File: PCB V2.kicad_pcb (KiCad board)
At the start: 2 copper layers, 17 parts, among them J1 Conector IR, J10 Conector ultrassonico esquerdo, J11 Conector ultrassonico central, J12 Conector ultrassonico direito, J13 Conector LED Extra, J14 Conector LORA, J15 ENCO_SW_Esq, J16 ENCO_SW_Dir, J18 LEDs, J2 Conector bluetooth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

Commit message: feat: finalizacao da versao 2 da pcb
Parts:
- added G***: LOGO, LOGO, F.Cu at (142.1, 37.9)
- added REF**: PinHeader_1x08_P2.54mm_Vertical, Connector_PinHeader_2.54mm:PinHeader_1x08_P2.54mm_Vertical, F.Cu at (157.4, 66.0)
- added REF**: MountingHole_3.2mm_M3, MountingHole:MountingHole_3.2mm_M3, F.Cu at (185.4, 36.6)
- added REF**: MountingHole_3.2mm_M3, MountingHole:MountingHole_3.2mm_M3, F.Cu at (185.4, 115.8)
- added REF**: PinHeader_1x08_P2.54mm_Vertical, Connector_PinHeader_2.54mm:PinHeader_1x08_P2.54mm_Vertical, F.Cu at (116.7, 114.3)
- added REF**: PinSocket_2x03_P2.54mm_Vertical, Connector_PinSocket_2.54mm:PinSocket_2x03_P2.54mm_Vertical, F.Cu at (154.9, 86.4)
- added REF**: PinHeader_1x08_P2.54mm_Vertical, Connector_PinHeader_2.54mm:PinHeader_1x08_P2.54mm_Vertical, F.Cu at (162.4, 114.3)
- added REF**: PinHeader_1x08_P2.54mm_Vertical, Connector_PinHeader_2.54mm:PinHeader_1x08_P2.54mm_Vertical, F.Cu at (134.5, 66.0)
- added REF**: MountingHole_3.2mm_M3, MountingHole:MountingHole_3.2mm_M3, F.Cu at (88.9, 36.6)
- added REF**: MountingHole_3.2mm_M3, MountingHole:MountingHole_3.2mm_M3, F.Cu at (88.9, 150.9)
- added REF**: PinHeader_1x10_P2.54mm_Vertical, Connector_PinHeader_2.54mm:PinHeader_1x10_P2.54mm_Vertical, F.Cu at (107.6, 66.0)
- added REF**: PinHeader_2x18_P2.54mm_Vertical, Connector_PinHeader_2.54mm:PinHeader_2x18_P2.54mm_Vertical, F.Cu at (182.8, 66.0)
- added REF**: PinHeader_1x08_P2.54mm_Vertical, Connector_PinHeader_2.54mm:PinHeader_1x08_P2.54mm_Vertical, F.Cu at (139.6, 114.3)
- J7, J8: moved to B.Cu
- moved J12 20.6 mm to (144.6, 50.8)
- moved J14 20.4 mm to (165.4, 50.8)
- moved R1 10.2 mm to (88.9, 58.2), turned to 0 degrees
- moved J7 2.03 mm to (99.1, 158.0), turned to 90 degrees
- moved J8 2.03 mm to (167.6, 158.0), turned to 90 degrees
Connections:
- J7 pad 1: 5V_Sen -> Earth
- J7 pad 2: Earth -> 5V_Sen
- J8 pad 1: 5V_Sen -> Earth
- J8 pad 2: Earth -> 5V_Sen
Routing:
- net Earth: track 80.4 -> 431.3 mm, vias 6 -> 19
- net 5V_Sen: track 90.7 -> 382.3 mm, vias 0 -> 14
- net IR2: track 0.00 -> 258.6 mm, vias 0 -> 8
- net ENCODER_Esq_1: track 0.00 -> 248.3 mm, vias 0 -> 8
- net IR1: track 0.00 -> 232.6 mm, vias 0 -> 4
- net LED_Extra: track 0.00 -> 172.0 mm, vias 0 -> 6
- net Servo: track 0.00 -> 136.3 mm, vias 0 -> 4
- net A_SDA: track 0.00 -> 135.2 mm, vias 0 -> 4
- net A_SCL: track 0.00 -> 134.3 mm, vias 0 -> 2
- net ENCODER_Dir_2: track 0.00 -> 130.3 mm, vias 0 -> 2
- net MD1: track 0.00 -> 129.8 mm, vias 0 -> 2
- net ENCODER_Dir_1: track 0.00 -> 124.8 mm, vias 0 -> 2
- net MD2: track 0.00 -> 124.5 mm, vias 0 -> 2
- net ME1: track 0.00 -> 120.9 mm, vias 0 -> 4
- net ME2: track 0.00 -> 116.5 mm, vias 0 -> 4
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- added copper zone on B.Cu, net Earth
- added copper zone on F.Cu, net Earth
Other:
- board outline added: 113.8 x 133.6 mm
- board text added: "+5V"
- board text added: "A"
- board text added: "B"
- board text added: "CONECTOR ACELEROMETRO"
- board text added: "CONECTOR BLUETOOTH"
- board text added: "CONECTOR DO SERVO"
- board text added: "CONECTOR ENCODER - DIR"
- board text added: "CONECTOR ENCODER - ESQ"
- board text added: "CONECTOR INFRAVERMELHO"
- board text added: "CONECTOR LED EXTRA"
- board text added: "CONECTOR LEDS FAROIS"
- board text added: "CONECTOR LORA"
- board text added: "CONECTOR ULTRASSONICO - CEN"
- board text added: "CONECTOR ULTRASSONICO - DIR"
- board text added: "CONECTOR ULTRASSONICO - ESQ"
- board text added: "ENTRADA BATERIA SENSORES"
- board text added: "FAROIS"
- board text added: "FREIOS"
- board text added: "GND"
- board text added: "M3"
- board text added: "PONTE H - DIR"
- board text added: "PONTE H - ESQ"
- board text added: "R 220 OHMS"
- board text added: "SERVO"
- board text added: "SETA DIR"
- board text added: "SETA ESQ"
- board text added: "SHIELD ARDUINO MEGA"
- board text added: "VCC"

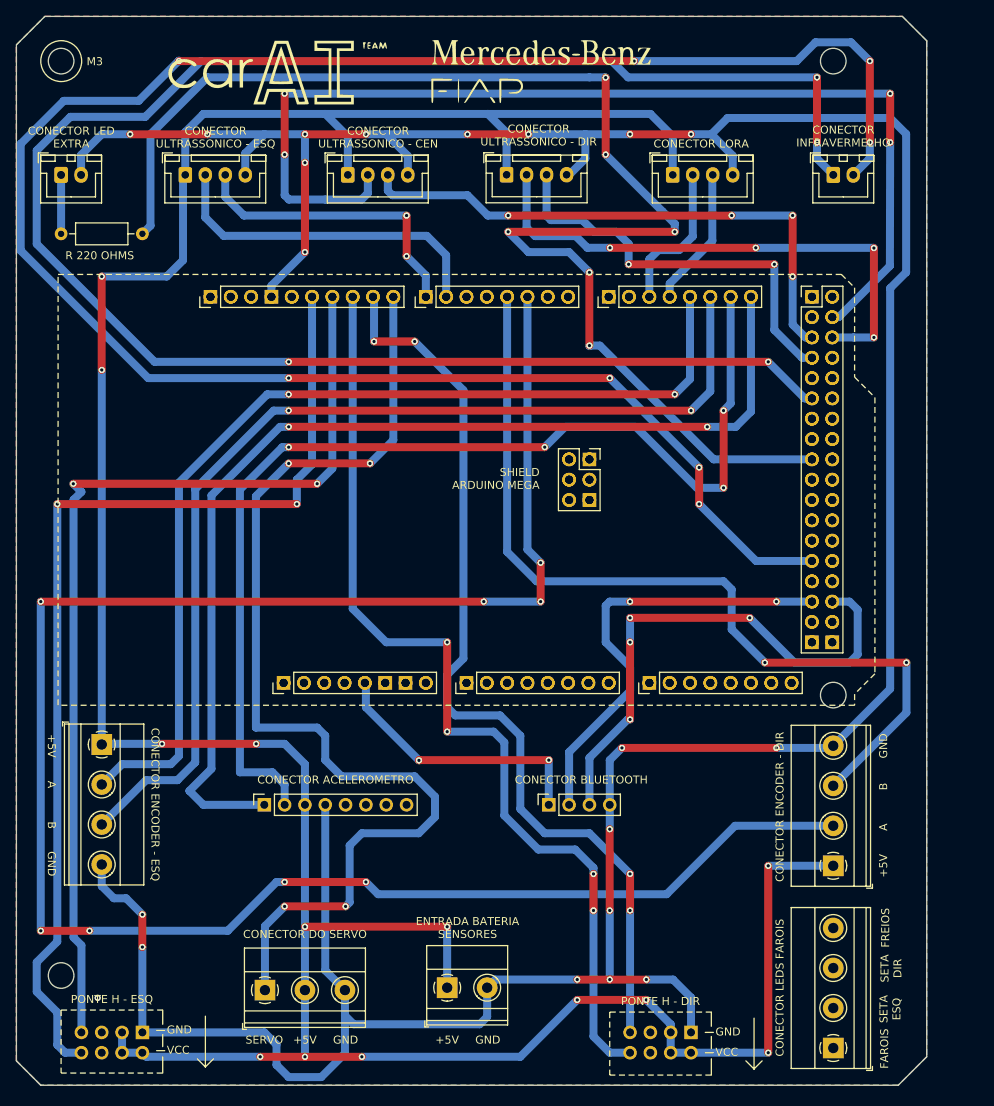
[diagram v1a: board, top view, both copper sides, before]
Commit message: fix: adição da entrada 8.4V do servo e outros
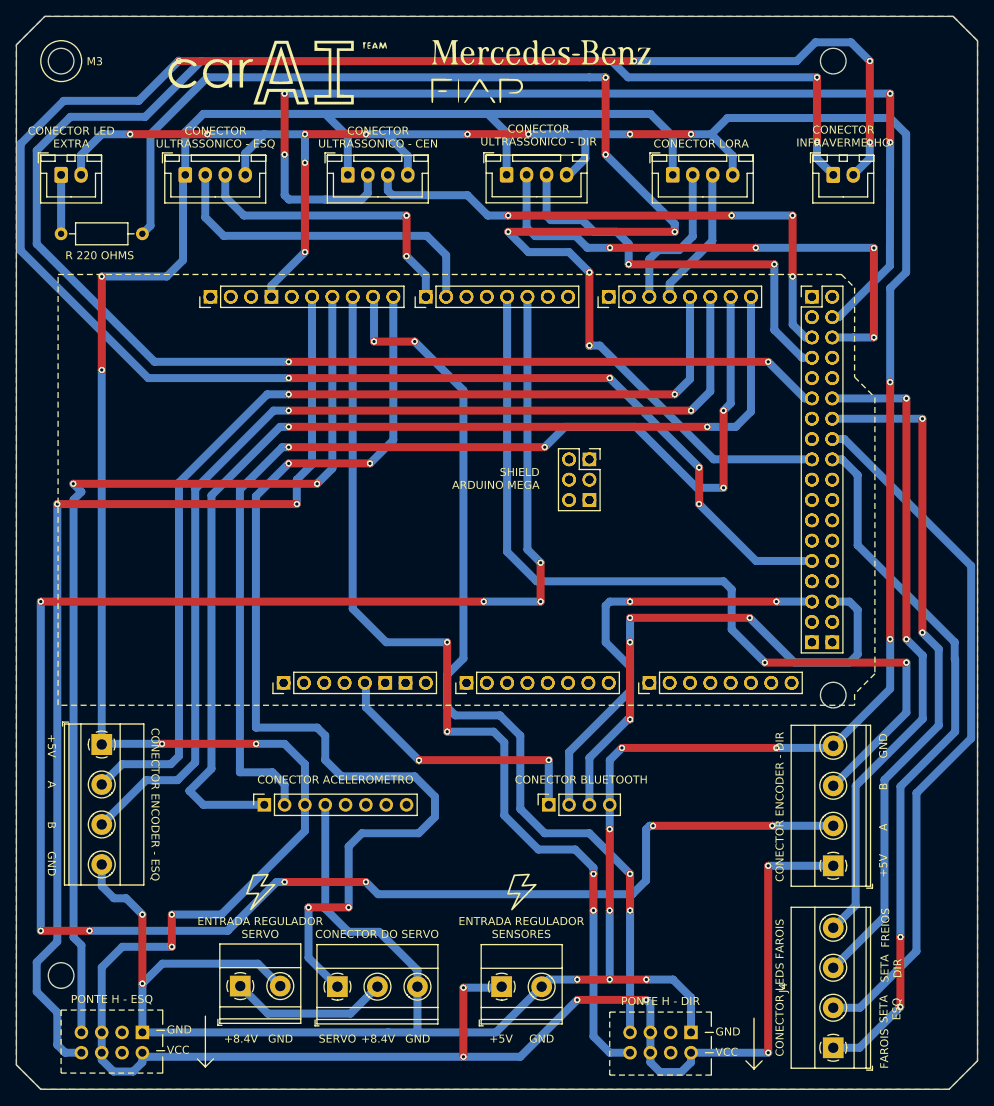
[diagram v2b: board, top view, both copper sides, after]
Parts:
- removed J18: LEDs, TerminalBlock_Phoenix:TerminalBlock_Phoenix_MKDS-1,5-4_1x04_P5.00mm_Horizontal
- added G***: LOGO, LOGO, F.Cu at (113.8, 140.5)
- added G***: LOGO, LOGO, F.Cu at (146.4, 140.5)
- added J4: LEDs, TerminalBlock_Phoenix:TerminalBlock_Phoenix_MKDS-1,5-4_1x04_P5.00mm_Horizontal, F.Cu at (185.4, 159.9)
- added J6: Conector alimentacao servo, TerminalBlock_Phoenix:TerminalBlock_Phoenix_MKDS-1,5-2_1x02_P5.00mm_Horizontal, F.Cu at (111.3, 152.2)
- moved REF** 22.9 mm to (134.5, 66.0)
- moved REF** 22.9 mm to (157.4, 66.0)
- moved J5 9.07 mm to (123.4, 152.3)
- moved J9 6.81 mm to (144.0, 152.3)
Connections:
- J5 pad 2: 5V_Sen -> 8.4V_Ser
- J7 pad 3: 5V_Sen -> unconnected-(J7-Pin_3-Pad3)
- J7 pad 4: 5V_Sen -> unconnected-(J7-Pin_4-Pad4)
- J7 pad 5: unconnected-(J7-Pin_5-Pad5) -> 5V_Sen
- J7 pad 6: unconnected-(J7-Pin_6-Pad6) -> 5V_Sen
- J8 pad 3: 5V_Sen -> unconnected-(J8-Pin_3-Pad3)
- J8 pad 4: 5V_Sen -> unconnected-(J8-Pin_4-Pad4)
- J8 pad 5: unconnected-(J8-Pin_5-Pad5) -> 5V_Sen
- J8 pad 6: unconnected-(J8-Pin_6-Pad6) -> 5V_Sen
- XA1 pad D31: unconnected-(XA1-PadD31) -> LED_Freios
- XA1 pad D32: Net-(J18-Pin_4) -> unconnected-(XA1-PadD32)
- XA1 pad D33: Net-(J18-Pin_3) -> LED_Seta_Dir
- XA1 pad D34: Net-(J18-Pin_2) -> unconnected-(XA1-PadD34)
- XA1 pad D35: Net-(J18-Pin_1) -> LED_Seta_Esq
- XA1 pad D37: unconnected-(XA1-PadD37) -> LED_Farois
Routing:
- net LED_Farois: track 0.00 -> 88.9 mm, vias 0 -> 2
- net LED_Seta_Esq: track 0.00 -> 88.3 mm
- net LED_Seta_Dir: track 0.00 -> 86.2 mm, vias 0 -> 2
- net LED_Freios: track 0.00 -> 80.9 mm, vias 0 -> 2
- net 8.4V_Ser: track 0.00 -> 20.0 mm
- net Earth: track 431.3 -> 447.0 mm, vias 19 -> 21
- net 5V_Sen: track 382.3 -> 395.7 mm, vias 14 -> 12
- net ENCODER_Esq_1: track 248.3 -> 252.1 mm, vias 8 -> 10
- net Servo: track 136.3 -> 133.6 mm
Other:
- board size 113.8 x 133.6 mm -> 120.1 x 134.1 mm
- board text added: "+8.4V"
- board text added: "ENTRADA REGULADOR SENSORES"
- board text added: "ENTRADA REGULADOR SERVO"
- board text removed: "ENTRADA BATERIA SENSORES"
